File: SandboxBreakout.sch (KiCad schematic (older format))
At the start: 6 parts

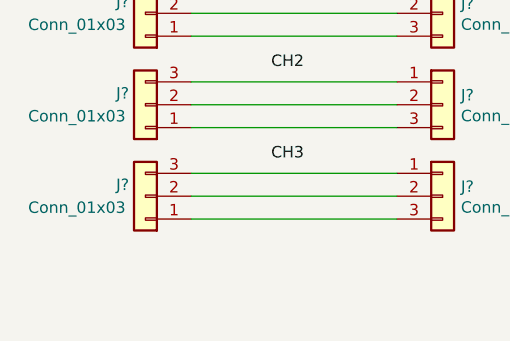
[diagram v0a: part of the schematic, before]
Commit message: Adding schematic.
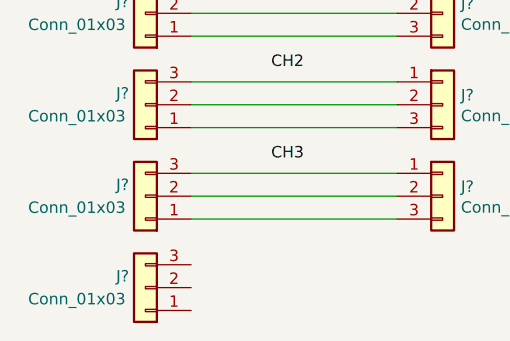
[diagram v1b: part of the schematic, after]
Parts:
- added J?: Conn_01x03, symbol Connector_Generic:Conn_01x03
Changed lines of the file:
@@
 Text Label 3050 1700 0    50   ~ 0
 CH3
+$Comp
+L Connector_Generic:Conn_01x03 J?
+U 1 1 616AC14C
+P 2500 2250
+F 0 "J?" H 2600 2200 50  0000 C CNN
+F 1 "Conn_01x03" H 2800 2300 50  0000 C CNN
+F 2 "" H 2500 2250 50  0001 C CNN
+F 3 "~" H 2500 2250 50  0001 C CNN
+	1    2500 2250
+	-1   0    0    1
+$EndComp
 $EndSCHEMATC

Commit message: test commit
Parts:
- added J5, J9: Conn_01x02, symbol Connector_Generic:Conn_01x02
- gave numbers to parts that had none: 7
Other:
- note added: "BUZZER"
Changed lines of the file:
@@
 	2700 1350 3600 1350
 $Comp
-L Connector_Generic:Conn_01x03 J?
+L Connector_Generic:Conn_01x03 J2
 U 1 1 616A49A7
 P 2500 1450
-F 0 "J?" H 2600 1400 50  0000 C CNN
+F 0 "J2" H 2600 1400 50  0000 C CNN
 F 1 "Conn_01x03" H 2800 1500 50  0000 C CNN
 F 2 "" H 2500 1450 50  0001 C CNN
@@
 $EndComp
 $Comp
-L Connector_Generic:Conn_01x03 J?
+L Connector_Generic:Conn_01x03 J7
 U 1 1 616A2D49
 P 3800 1450
-F 0 "J?" H 3880 1492 50  0000 L CNN
+F 0 "J7" H 3880 1492 50  0000 L CNN
 F 1 "Conn_01x03" H 3880 1401 50  0000 L CNN
 F 2 "" H 3800 1450 50  0001 C CNN
@@
 $EndComp
 $Comp
-L Connector_Generic:Conn_01x03 J?
+L Connector_Generic:Conn_01x03 J1
 U 1 1 616A1CEF
 P 2500 1050
-F 0 "J?" H 2600 1000 50  0000 C CNN
+F 0 "J1" H 2600 1000 50  0000 C CNN
 F 1 "Conn_01x03" H 2800 1100 50  0000 C CNN
 F 2 "" H 2500 1050 50  0001 C CNN
@@
 $EndComp
 $Comp
-L Connector_Generic:Conn_01x03 J?
+L Connector_Generic:Conn_01x03 J6
 U 1 1 616A09CD
 P 3800 1050
-F 0 "J?" H 3880 1092 50  0000 L CNN
+F 0 "J6" H 3880 1092 50  0000 L CNN
 F 1 "Conn_01x03" H 3880 1001 50  0000 L CNN
 F 2 "" H 3800 1050 50  0001 C CNN
@@
 $EndComp
 $Comp
-L Connector_Generic:Conn_01x03 J?
+L Connector_Generic:Conn_01x03 J3
 U 1 1 616A9CD6
 P 2500 1850
-F 0 "J?" H 2600 1800 50  0000 C CNN
+F 0 "J3" H 2600 1800 50  0000 C CNN
 F 1 "Conn_01x03" H 2800 1900 50  0000 C CNN
 F 2 "" H 2500 1850 50  0001 C CNN
@@
 $EndComp
 $Comp
-L Connector_Generic:Conn_01x03 J?
+L Connector_Generic:Conn_01x03 J8
 U 1 1 616A9FAA
 P 3800 1850
-F 0 "J?" H 3880 1892 50  0000 L CNN
+F 0 "J8" H 3880 1892 50  0000 L CNN
 F 1 "Conn_01x03" H 3880 1801 50  0000 L CNN
 F 2 "" H 3800 1850 50  0001 C CNN
@@
 CH3
 $Comp
-L Connector_Generic:Conn_01x03 J?
+L Connector_Generic:Conn_01x03 J4
 U 1 1 616AC14C
 P 2500 2250
-F 0 "J?" H 2600 2200 50  0000 C CNN
+F 0 "J4" H 2600 2200 50  0000 C CNN
 F 1 "Conn_01x03" H 2800 2300 50  0000 C CNN
 F 2 "" H 2500 2250 50  0001 C CNN
@@
 	-1   0    0    1
 $EndComp
+$Comp
+L Connector_Generic:Conn_01x02 J9
+U 1 1 616C2167
+P 3800 3200
+F 0 "J9" H 3880 3192 50  0000 L CNN
+F 1 "Conn_01x02" H 3880 3101 50  0000 L CNN
+F 2 "" H 3800 3200 50  0001 C CNN
+F 3 "~" H 3800 3200 50  0001 C CNN
+	1    3800 3200
+	1    0    0    -1
+$EndComp
+$Comp
+L Connector_Generic:Conn_01x02 J5
+U 1 1 616C163A
+P 2500 3200
+F 0 "J5" H 2580 3192 50  0000 L CNN
+F 1 "Conn_01x02" H 2580 3101 50  0000 L CNN
+F 2 "" H 2500 3200 50  0001 C CNN
+F 3 "~" H 2500 3200 50  0001 C CNN
+	1    2500 3200
+	1    0    0    -1
+$EndComp
+Text Notes 2950 3000 0    59   ~ 0
+BUZZER
 $EndSCHEMATC

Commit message: pixhawk connections added
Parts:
- removed J4: Conn_01x03, symbol Connector_Generic:Conn_01x03
- added J? (x32): Conn_01x03, symbol Connector_Generic:Conn_01x03
- added J? (x10): Conn_01x06, symbol Connector_Generic:Conn_01x06
- added J? (x2): Conn_01x05, symbol Connector_Generic:Conn_01x05
- added J? (x6): Conn_01x04, symbol Connector_Generic:Conn_01x04
- added J? (x2): Conn_01x07, symbol Connector_Generic:Conn_01x07
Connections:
- net at J5.1 (Pin_1): now also J9.1 (Pin_1)
- net at J5.2 (Pin_2): now also J9.2 (Pin_2)
- new net: J?.1 (Pin_1), J?.3 (Pin_3) (x32)
- new net: J?.2 (Pin_2), J?.2 (Pin_2) (x26)
- new net: J?.1 (Pin_1), J?.1 (Pin_1) (x10)
- new net: J?.3 (Pin_3), J?.3 (Pin_3) (x10)
- new net: J?.4 (Pin_4), J?.4 (Pin_4) (x10)
- new net: J?.5 (Pin_5), J?.5 (Pin_5) (x7)
- new net: J?.6 (Pin_6), J?.6 (Pin_6) (x6)
- new net: J?.7 (Pin_7), J?.7 (Pin_7)
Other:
- note removed: "BUZZER"
- moved on the sheet: J5, J9

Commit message: Started Pcbnew, servo connectors all scrambled
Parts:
- removed J5, J9: Conn_01x02, symbol Connector_Generic:Conn_01x02
- removed J? (x24): Conn_01x03, symbol Connector_Generic:Conn_01x03
- added Servo10, Servo11, Servo12, Servo13, Servo14, Servo15, Servo16, Servo17, Servo18, Servo19, Servo20, Servo21, Servo22, Servo23, Servo24, Servo25, Servo26, Servo27, Servo28, Servo29, Servo30, Servo31, Servo32, Servo9: Conn_01x03, Connector_PinHeader_2.54mm:PinHeader_1x03_P2.54mm_Vertical, symbol Connector_Generic:Conn_01x03
- 12C_1, 12C_2, Can1, Can2, USB1, USB2: renamed from J?; footprint (none) -> Connector_JST:JST_GH_BM04B-GHS-TBT_1x04-1MP_P1.25mm_Vertical
- ADC3.3_1, ADC3.3_2: renamed from J?; footprint (none) -> Connector_JST:JST_GH_BM05B-GHS-TBT_1x05-1MP_P1.25mm_Vertical
- ADC6.6_1, ADC6.6_2, SPKT1, SPKT2, Switch1, Switch2: renamed from J?; footprint (none) -> Connector_JST:JST_GH_BM03B-GHS-TBT_1x03-1MP_P1.25mm_Vertical
- GPS1, GPS2, Pow1, Pow2, Serial1, Serial2, Telem1, Telem2, Telem3, Telem4: renamed from J?; footprint (none) -> Connector_JST:JST_GH_BM06B-GHS-TBT_1x06-1MP_P1.25mm_Vertical
- SPI1, SPI2: renamed from J?; footprint (none) -> Connector_JST:JST_GH_BM07B-GHS-TBT_1x07-1MP_P1.25mm_Vertical
- Servo1: renamed from J1; footprint (none) -> Connector_PinHeader_2.54mm:PinHeader_1x03_P2.54mm_Vertical
- Servo2: renamed from J6; footprint (none) -> Connector_PinHeader_2.54mm:PinHeader_1x03_P2.54mm_Vertical
- Servo3: renamed from J2; footprint (none) -> Connector_PinHeader_2.54mm:PinHeader_1x03_P2.54mm_Vertical
- Servo4: renamed from J7; footprint (none) -> Connector_PinHeader_2.54mm:PinHeader_1x03_P2.54mm_Vertical
- Servo5: renamed from J3; footprint (none) -> Connector_PinHeader_2.54mm:PinHeader_1x03_P2.54mm_Vertical
- Servo6: renamed from J8; footprint (none) -> Connector_PinHeader_2.54mm:PinHeader_1x03_P2.54mm_Vertical
- Servo7, Servo8: renamed from J?; footprint (none) -> Connector_PinHeader_2.54mm:PinHeader_1x03_P2.54mm_Vertical
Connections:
- net at Servo2.1 (Pin_1): now also Servo1.1 (Pin_1); no longer Servo1.3 (Pin_3)
- net at Servo2.3 (Pin_3): now also Servo1.3 (Pin_3); no longer Servo1.1 (Pin_1)
- net at Servo4.1 (Pin_1): now also Servo3.1 (Pin_1); no longer Servo3.3 (Pin_3)
- net at Servo4.3 (Pin_3): now also Servo3.3 (Pin_3); no longer Servo3.1 (Pin_1)
- net at Servo5.1 (Pin_1): now also Servo6.1 (Pin_1); no longer Servo6.3 (Pin_3)
- net at Servo5.3 (Pin_3): now also Servo6.3 (Pin_3); no longer Servo6.1 (Pin_1)
- net at Servo7.1 (Pin_1): now also Servo8.1 (Pin_1); no longer Servo8.3 (Pin_3)
- net at Servo7.3 (Pin_3): now also Servo8.3 (Pin_3); no longer Servo8.1 (Pin_1)
- net at Switch1.1 (Pin_1): now also Switch2.1 (Pin_1); no longer Switch2.3 (Pin_3)
- net at Switch1.3 (Pin_3): now also Switch2.3 (Pin_3); no longer Switch2.1 (Pin_1)
- net at SPKT1.1 (Pin_1): now also SPKT2.1 (Pin_1); no longer SPKT2.3 (Pin_3)
- net at SPKT1.3 (Pin_3): now also SPKT2.3 (Pin_3); no longer SPKT2.1 (Pin_1)
- net at ADC6.6_2.1 (Pin_1): now also ADC6.6_1.1 (Pin_1); no longer ADC6.6_1.3 (Pin_3)
- net at ADC6.6_2.3 (Pin_3): now also ADC6.6_1.3 (Pin_3); no longer ADC6.6_1.1 (Pin_1)
- new net: Servo11.1 (Pin_1), Servo12.1 (Pin_1)
- new net: Servo11.2 (Pin_2), Servo12.2 (Pin_2)
- new net: Servo11.3 (Pin_3), Servo12.3 (Pin_3)
- new net: Servo10.1 (Pin_1), Servo9.1 (Pin_1)
- new net: Servo10.2 (Pin_2), Servo9.2 (Pin_2)
- new net: Servo10.3 (Pin_3), Servo9.3 (Pin_3)
- new net: Servo19.1 (Pin_1), Servo20.1 (Pin_1)
- new net: Servo19.2 (Pin_2), Servo20.2 (Pin_2)
- new net: Servo19.3 (Pin_3), Servo20.3 (Pin_3)
- new net: Servo17.1 (Pin_1), Servo18.1 (Pin_1)
- new net: Servo17.2 (Pin_2), Servo18.2 (Pin_2)
- new net: Servo17.3 (Pin_3), Servo18.3 (Pin_3)
- new net: Servo15.1 (Pin_1), Servo16.1 (Pin_1)
- new net: Servo15.2 (Pin_2), Servo16.2 (Pin_2)
- new net: Servo15.3 (Pin_3), Servo16.3 (Pin_3)
- new net: Servo13.1 (Pin_1), Servo14.1 (Pin_1)
- new net: Servo13.2 (Pin_2), Servo14.2 (Pin_2)
- new net: Servo13.3 (Pin_3), Servo14.3 (Pin_3)
- new net: Servo23.1 (Pin_1), Servo24.1 (Pin_1)
- new net: Servo23.2 (Pin_2), Servo24.2 (Pin_2)
- new net: Servo23.3 (Pin_3), Servo24.3 (Pin_3)
- new net: Servo21.1 (Pin_1), Servo22.1 (Pin_1)
- new net: Servo21.2 (Pin_2), Servo22.2 (Pin_2)
- new net: Servo21.3 (Pin_3), Servo22.3 (Pin_3)
- new net: Servo27.1 (Pin_1), Servo28.1 (Pin_1)
- new net: Servo27.2 (Pin_2), Servo28.2 (Pin_2)
- new net: Servo27.3 (Pin_3), Servo28.3 (Pin_3)
- new net: Servo25.1 (Pin_1), Servo26.1 (Pin_1)
- new net: Servo25.2 (Pin_2), Servo26.2 (Pin_2)
- new net: Servo25.3 (Pin_3), Servo26.3 (Pin_3)
- new net: Servo31.1 (Pin_1), Servo32.1 (Pin_1)
- new net: Servo31.2 (Pin_2), Servo32.2 (Pin_2)
- new net: Servo31.3 (Pin_3), Servo32.3 (Pin_3)
- new net: Servo29.1 (Pin_1), Servo30.1 (Pin_1)
- new net: Servo29.2 (Pin_2), Servo30.2 (Pin_2)
- new net: Servo29.3 (Pin_3), Servo30.3 (Pin_3)

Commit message: Board Draft 1.0
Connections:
- net at Servo1.2 (Pin_2), Servo2.2 (Pin_2): now also Servo10.2 (Pin_2), Servo11.2 (Pin_2), Servo12.2 (Pin_2), Servo13.2 (Pin_2), Servo14.2 (Pin_2), Servo15.2 (Pin_2), Servo16.2 (Pin_2), Servo17.2 (Pin_2), Servo18.2 (Pin_2), Servo19.2 (Pin_2), Servo20.2 (Pin_2), Servo21.2 (Pin_2), Servo22.2 (Pin_2), Servo23.2 (Pin_2), Servo24.2 (Pin_2), Servo25.2 (Pin_2), Servo26.2 (Pin_2), Servo27.2 (Pin_2), Servo28.2 (Pin_2), Servo29.2 (Pin_2), Servo3.2 (Pin_2), Servo30.2 (Pin_2), Servo31.2 (Pin_2), Servo32.2 (Pin_2), Servo4.2 (Pin_2), Servo5.2 (Pin_2), Servo6.2 (Pin_2), Servo7.2 (Pin_2), Servo8.2 (Pin_2), Servo9.2 (Pin_2)
- net at Servo1.3 (Pin_3), Servo2.3 (Pin_3): now also Servo10.3 (Pin_3), Servo11.3 (Pin_3), Servo12.3 (Pin_3), Servo13.3 (Pin_3), Servo14.3 (Pin_3), Servo15.3 (Pin_3), Servo16.3 (Pin_3), Servo17.3 (Pin_3), Servo18.3 (Pin_3), Servo19.3 (Pin_3), Servo20.3 (Pin_3), Servo21.3 (Pin_3), Servo22.3 (Pin_3), Servo23.3 (Pin_3), Servo24.3 (Pin_3), Servo25.3 (Pin_3), Servo26.3 (Pin_3), Servo27.3 (Pin_3), Servo28.3 (Pin_3), Servo29.3 (Pin_3), Servo3.3 (Pin_3), Servo30.3 (Pin_3), Servo31.3 (Pin_3), Servo32.3 (Pin_3), Servo4.3 (Pin_3), Servo5.3 (Pin_3), Servo6.3 (Pin_3), Servo7.3 (Pin_3), Servo8.3 (Pin_3), Servo9.3 (Pin_3)
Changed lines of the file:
@@
 ADC6.6V
 Wire Wire Line
-	2700 2400 3600 2400
-Wire Wire Line
-	2700 1950 3600 1950
-Wire Wire Line
-	2700 1550 3600 1550
+	2700 2400 2800 2400
+Wire Wire Line
+	2700 1950 2800 1950
+Wire Wire Line
+	2700 1550 2800 1550
 $Comp
 L Connector_Generic:Conn_01x03 Servo8
@@
 $EndComp
 Wire Wire Line
-	2700 1150 3600 1150
+	2700 1150 2800 1150
 $Comp
 L Connector_Generic:Conn_01x03 Servo2
@@
 AUX6
 Wire Wire Line
-	2700 3300 3600 3300
-Wire Wire Line
-	2700 2850 3600 2850
+	2700 3300 2800 3300
+Wire Wire Line
+	2700 2850 2800 2850
 $Comp
 L Connector_Generic:Conn_01x03 Servo12
@@
 MAIN4
 Wire Wire Line
-	2700 5000 3600 5000
-Wire Wire Line
-	2700 4550 3600 4550
-Wire Wire Line
-	2700 4150 3600 4150
+	2700 5000 2800 5000
+Wire Wire Line
+	2700 4550 2800 4550
+Wire Wire Line
+	2700 4150 2800 4150
 $Comp
 L Connector_Generic:Conn_01x03 Servo20
@@
 $EndComp
 Wire Wire Line
-	2700 3750 3600 3750
+	2700 3750 2800 3750
 $Comp
 L Connector_Generic:Conn_01x03 Servo14
@@
 MAIN6
 Wire Wire Line
-	2700 5900 3600 5900
-Wire Wire Line
-	2700 5450 3600 5450
+	2700 5900 2800 5900
+Wire Wire Line
+	2700 5450 2800 5450
 $Comp
 L Connector_Generic:Conn_01x03 Servo24
@@
 MAIN8
 Wire Wire Line
-	2700 6750 3600 6750
-Wire Wire Line
-	2700 6300 3600 6300
+	2700 6750 2800 6750
+Wire Wire Line
+	2700 6300 2800 6300
 Wire Wire Line
 	2700 6100 3600 6100
@@
 RCIN
 Wire Wire Line
-	2700 7700 3600 7700
-Wire Wire Line
-	2700 7250 3600 7250
+	2700 7700 2800 7700
+Wire Wire Line
+	2700 7250 2800 7250
 $Comp
 L Connector_Generic:Conn_01x03 Servo32
@@
 	2700 1350 3600 1350
 Wire Wire Line
-	2700 1050 3600 1050
-Wire Wire Line
-	2700 1450 3600 1450
-Wire Wire Line
-	2700 1850 3600 1850
-Wire Wire Line
-	2700 2300 3600 2300
-Wire Wire Line
-	2700 2750 3600 2750
-Wire Wire Line
-	2700 3200 3600 3200
-Wire Wire Line
-	2700 3650 3600 3650
-Wire Wire Line
-	2700 4050 3600 4050
-Wire Wire Line
-	2700 4450 3600 4450
-Wire Wire Line
-	2700 4900 3600 4900
-Wire Wire Line
-	2700 5350 3600 5350
-Wire Wire Line
-	2700 5800 3600 5800
-Wire Wire Line
-	2700 6200 3600 6200
-Wire Wire Line
-	2700 6650 3600 6650
-Wire Wire Line
-	2700 7150 3600 7150
-Wire Wire Line
-	2700 7600 3600 7600
+	2700 2750 2950 2750
+Wire Wire Line
+	2700 3200 2950 3200
+Wire Wire Line
+	2700 3650 2950 3650
+Wire Wire Line
+	2700 4050 2950 4050
+Wire Wire Line
+	2700 4450 2950 4450
+Wire Wire Line
+	2700 4900 2950 4900
+Wire Wire Line
+	2700 5350 2950 5350
+Wire Wire Line
+	2700 5800 2950 5800
+Wire Wire Line
+	2700 6200 2950 6200
+Wire Wire Line
+	2700 6650 2950 6650
+Wire Wire Line
+	2700 7150 2950 7150
+Wire Wire Line
+	2700 7600 2950 7600
+Wire Wire Line
+	2800 1150 2800 1550
+Connection ~ 2800 1150
+Wire Wire Line
+	2800 1150 3600 1150
+Connection ~ 2800 1550
+Wire Wire Line
+	2800 1550 3600 1550
+Wire Wire Line
+	2800 1550 2800 1950
+Connection ~ 2800 1950
+Wire Wire Line
+	2800 1950 3600 1950
+Wire Wire Line
+	2800 2400 2800 1950
+Connection ~ 2800 2400
+Wire Wire Line
+	2800 2400 3600 2400
+Wire Wire Line
+	2800 2400 2800 2850
+Connection ~ 2800 2850
+Wire Wire Line
+	2800 2850 3600 2850
+Wire Wire Line
+	2800 3300 2800 2850
+Connection ~ 2800 3300
+Wire Wire Line
+	2800 3300 3600 3300
+Wire Wire Line
+	2800 3300 2800 3750
+Connection ~ 2800 3750
+Wire Wire Line
+	2800 3750 3600 3750
+Wire Wire Line
+	2800 3750 2800 4150
+Connection ~ 2800 4150
+Wire Wire Line
+	2800 4150 3600 4150
+Wire Wire Line
+	2800 4150 2800 4550
+Connection ~ 2800 4550
+Wire Wire Line
+	2800 4550 3600 4550
+Wire Wire Line
+	2800 4550 2800 5000
+Connection ~ 2800 5000
+Wire Wire Line
+	2800 5000 3600 5000
+Wire Wire Line
+	2800 5000 2800 5450
+Connection ~ 2800 5450
+Wire Wire Line
+	2800 5450 3600 5450
+Wire Wire Line
+	2800 5450 2800 5900
+Connection ~ 2800 5900
+Wire Wire Line
+	2800 5900 3600 5900
+Wire Wire Line
+	2800 5900 2800 6300
+Connection ~ 2800 6300
+Wire Wire Line
+	2800 6300 3600 6300
+Wire Wire Line
+	2800 6300 2800 6750
+Connection ~ 2800 6750
+Wire Wire Line
+	2800 6750 3600 6750
+Wire Wire Line
+	2800 6750 2800 7250
+Connection ~ 2800 7250
+Wire Wire Line
+	2800 7250 3600 7250
+Wire Wire Line
+	2800 7250 2800 7700
+Connection ~ 2800 7700
+Wire Wire Line
+	2800 7700 3600 7700
+Wire Wire Line
+	2950 1050 2950 1450
+Wire Wire Line
+	2700 1050 2950 1050
+Wire Wire Line
+	2950 1050 3600 1050
+Connection ~ 2950 1050
+Wire Wire Line
+	2700 1450 2950 1450
+Wire Wire Line
+	2950 1450 3600 1450
+Connection ~ 2950 1450
+Wire Wire Line
+	2950 1450 2950 1850
+Wire Wire Line
+	2700 1850 2950 1850
+Wire Wire Line
+	2950 1850 3600 1850
+Connection ~ 2950 1850
+Wire Wire Line
+	2950 1850 2950 2300
+Wire Wire Line
+	2700 2300 2950 2300
+Wire Wire Line
+	2950 2300 3600 2300
+Connection ~ 2950 2300
+Wire Wire Line
+	2950 2300 2950 2750
+Connection ~ 2950 2750
+Wire Wire Line
+	2950 2750 3600 2750
+Wire Wire Line
+	2950 2750 2950 3200
+Connection ~ 2950 3200
+Wire Wire Line
+	2950 3200 3600 3200
+Wire Wire Line
+	2950 3200 2950 3650
+Connection ~ 2950 3650
+Wire Wire Line
+	2950 3650 3600 3650
+Wire Wire Line
+	2950 3650 2950 4050
+Connection ~ 2950 4050
+Wire Wire Line
+	2950 4050 3600 4050
+Wire Wire Line
+	2950 4050 2950 4450
+Connection ~ 2950 4450
+Wire Wire Line
+	2950 4450 3600 4450
+Wire Wire Line
+	2950 4450 2950 4900
+Connection ~ 2950 4900
+Wire Wire Line
+	2950 4900 3600 4900
+Wire Wire Line
+	2950 4900 2950 5350
+Connection ~ 2950 5350
+Wire Wire Line
+	2950 5350 3600 5350
+Wire Wire Line
+	2950 5350 2950 5800
+Connection ~ 2950 5800
+Wire Wire Line
+	2950 5800 3600 5800
+Wire Wire Line
+	2950 5800 2950 6200
+Connection ~ 2950 6200
+Wire Wire Line
+	2950 6200 3600 6200
+Wire Wire Line
+	2950 6200 2950 6650
+Connection ~ 2950 6650
+Wire Wire Line
+	2950 6650 3600 6650
+Wire Wire Line
+	2950 6650 2950 7150
+Connection ~ 2950 7150
+Wire Wire Line
+	2950 7150 3600 7150
+Wire Wire Line
+	2950 7150 2950 7600
+Connection ~ 2950 7600
+Wire Wire Line
+	2950 7600 3600 7600
+Text Label 3500 700  0    50   ~ 0
+1-Signal,2-Power,3-Ground
 $EndSCHEMATC

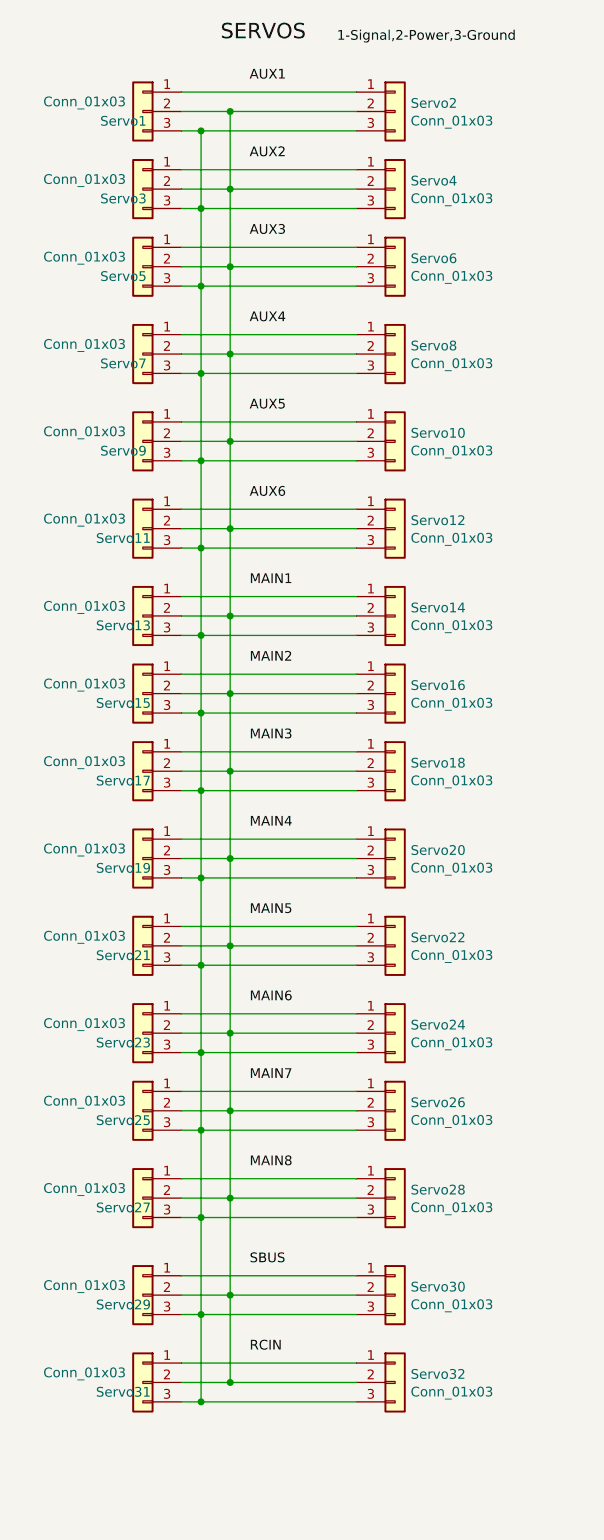
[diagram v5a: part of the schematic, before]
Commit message: Updated labels
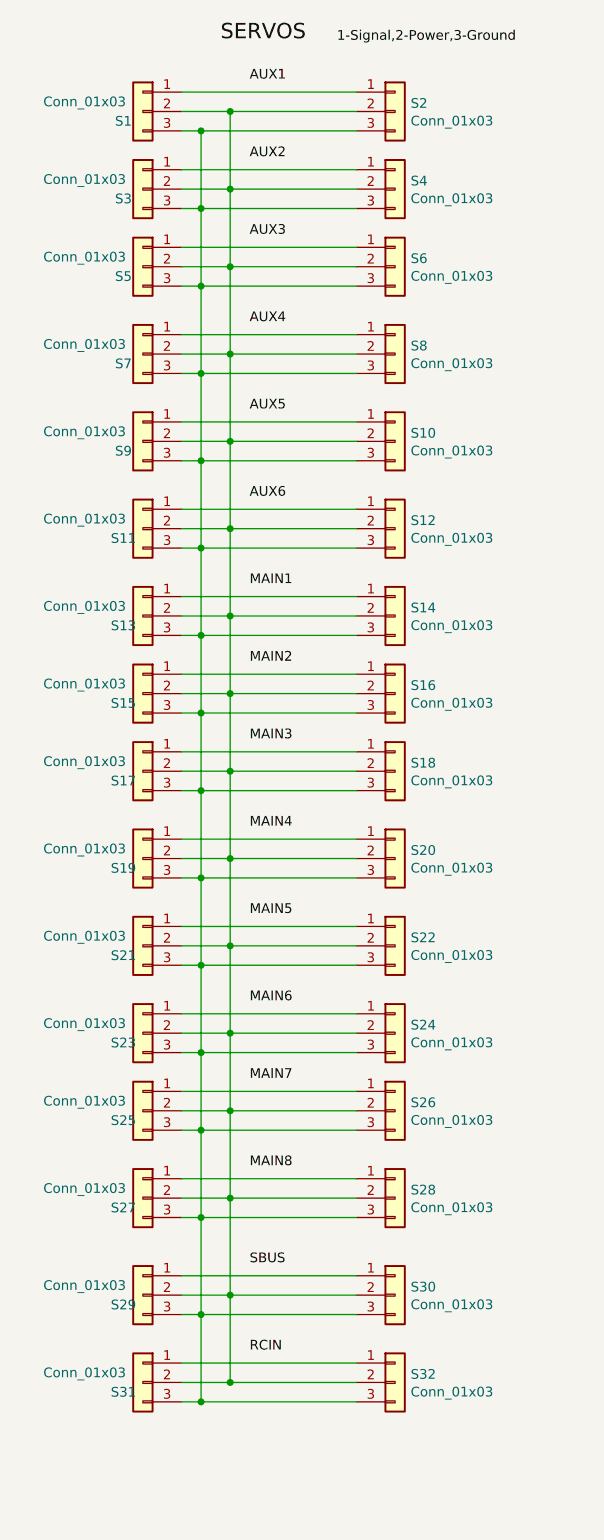
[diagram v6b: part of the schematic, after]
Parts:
- renumbered Servo1 to S1, Servo10 to S10, Servo11 to S11, Servo12 to S12, Servo13 to S13, Servo14 to S14, Servo15 to S15, Servo16 to S16, Servo17 to S17, Servo18 to S18, Servo19 to S19, Servo2 to S2, Servo20 to S20, Servo21 to S21, Servo22 to S22, Servo23 to S23, Servo24 to S24, Servo25 to S25, Servo26 to S26, Servo27 to S27, Servo28 to S28, Servo29 to S29, Servo3 to S3, Servo30 to S30, Servo31 to S31, Servo32 to S32, Servo4 to S4, Servo5 to S5, Servo6 to S6, Servo7 to S7, Servo8 to S8, Servo9 to S9
